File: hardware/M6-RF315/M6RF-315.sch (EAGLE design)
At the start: 38 parts, among them J1 CON-71439-2164, M1 MOUNT-HOLE3.3, M2 MOUNT-HOLE3.3, M3 MOUNT-HOLE3.3, M4 MOUNT-HOLE3.3, M5 FIDUCIAL1X2, M6 FIDUCIAL1X2, M7 FIDUCIAL1X2, M8 FIDUCIAL1X2, U1 CC1101RTKR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

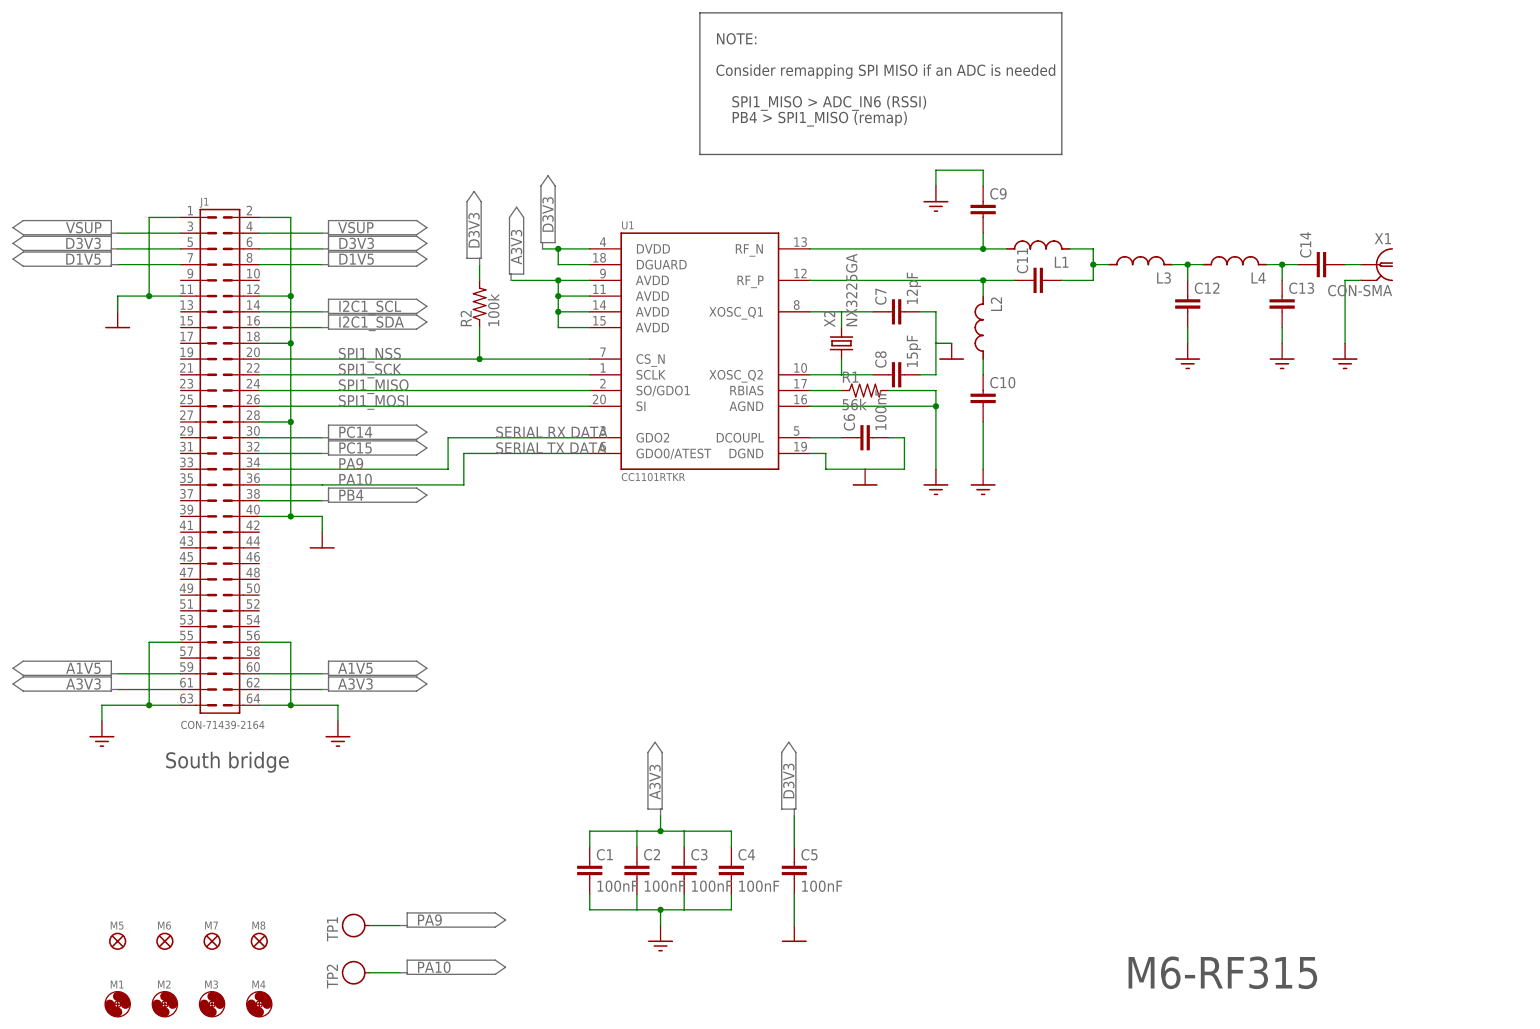
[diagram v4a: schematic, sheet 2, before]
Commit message: Modified GPIO-serial data connection, added LEDs, updated and cleaned up the library, defined antenna circuit component values and added datasheet..
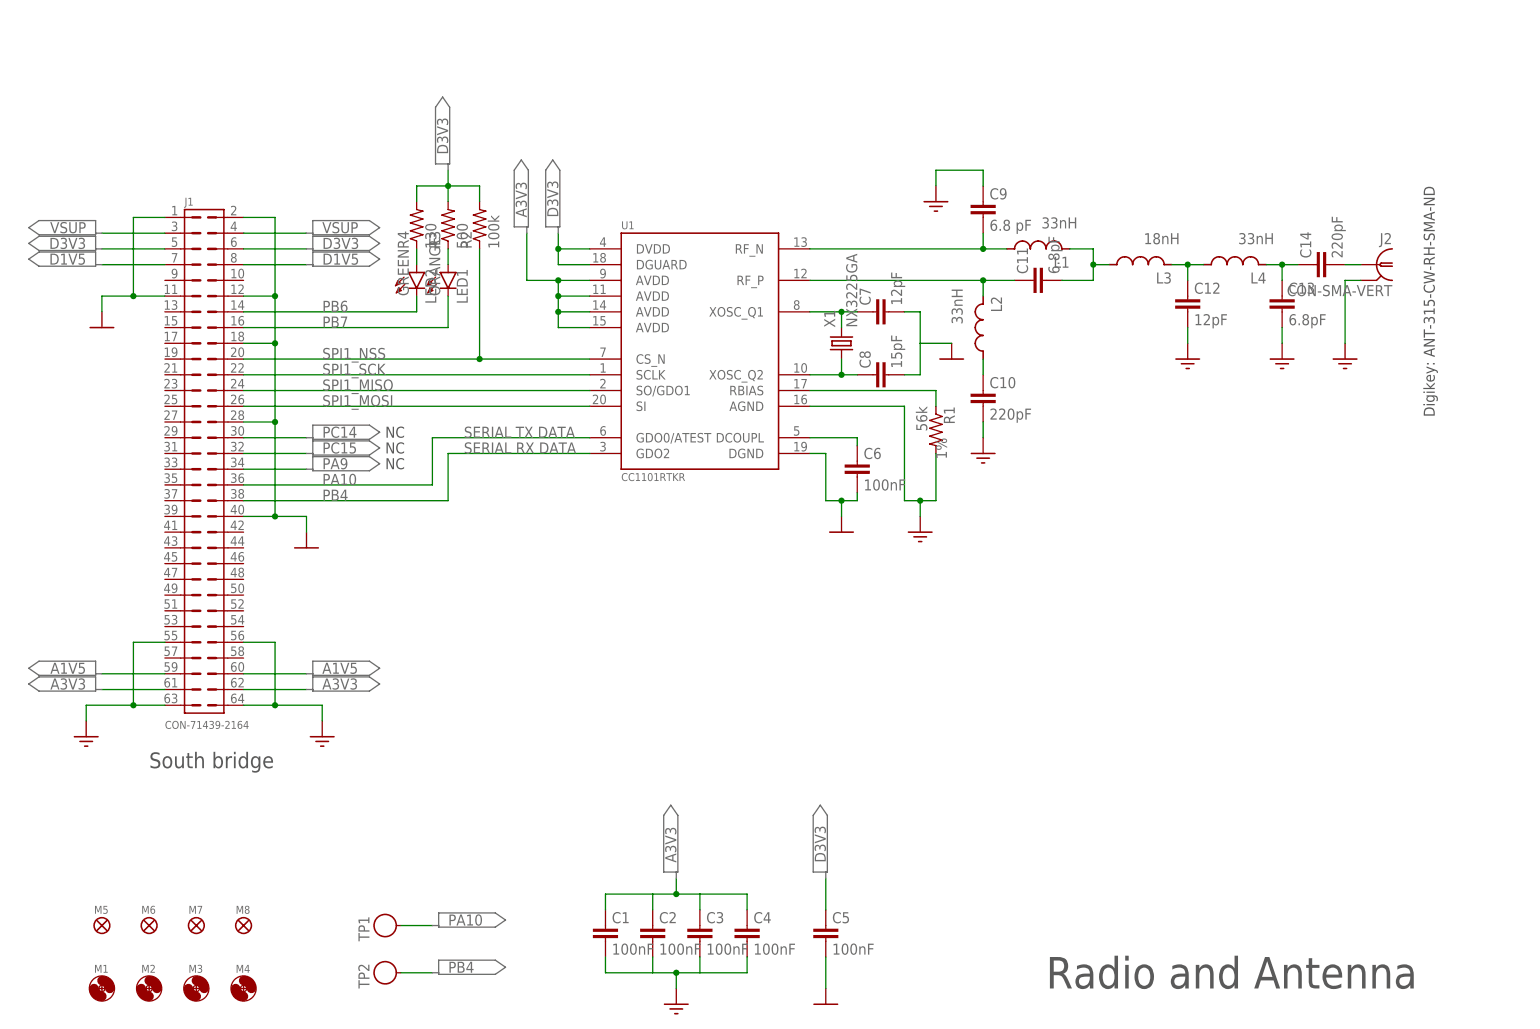
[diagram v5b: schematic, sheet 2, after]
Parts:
- removed X2: NX3225GA, M6-RF315:NX3225GA
- added J2: CON-SMA-VERT, M6-RF315:CON-SMA-VERT
- added LED1, LED2: (no value), M6-RF315:LED0603
- added R3: 500, M6-RF315:R0603
- added R4: 130, M6-RF315:R0603
- C10: value (none) -> 220pF; FUNCTION (none) -> RF balun DC blocking capacitor
- C11: value (none) -> 6.8pF; FUNCTION (none) -> RF balun/matching capacitors
- C12: value (none) -> 12pF; FUNCTION (none) -> RF LC filter/matching filter capacitor
- C13: value (none) -> 6.8pF; FUNCTION (none) -> RF LC filter/matching capacitor
- C14: value (none) -> 220pF; FUNCTION (none) -> RF LC filter DC blocking capacitor
- C9: value (none) -> 6.8 pF; FUNCTION (none) -> RF balun/matching capacitor
- L1, L2: value (none) -> 33nH; FUNCTION (none) -> RF balun/matching inductor
- L3: value (none) -> 18nH; FUNCTION (none) -> RF LC filter/matching filter inductor
- L4: value (none) -> 33nH; FUNCTION (none) -> RF LC filter/matching filter inductor
- R1: TOLERANCE (none) -> 1%
- X1: value CON-SMA -> NX3225GA; device M6-RF315:CON-SMA -> M6-RF315:NX3225GA
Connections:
- removed net I2C1_SCL: J1.14
- removed net I2C1_SDA: J1.16
- removed net N$5: C6.2
- new net N$19: LED2.A, R4.1
- new net PB6: J1.14, LED2.C
- new net PB7: J1.16, LED1.C
- net AGND: now also J2G$1.GND; no longer X1G$1.GND
- net D3V3: now also R3.2, R4.2
- net DGND: now also C6.2
- net N$1: now also LED1.A, R3.1; no longer J1.34, U1.GDO2
- net N$12: now also J2G$1.1; no longer X1G$1.1
- net N$6: now also X1.1; no longer X2.1
- net N$7: now also X1.2; no longer X2.2
- net PA10: now also TP1.1, U1.GDO0/ATEST; no longer TP2.1
- net PA9: now also J1.34; no longer TP1.1, U1.GDO0/ATEST
- net PB4: now also TP2.1, U1.GDO2
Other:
- note added: "- Check BOM against CC1101 reference BOM for 315 MHz"
- note added: "- Create BOM file"
- note added: "- Route PCB design"
- note added: "NC"
- note removed: "- Antenna matching circuit values"
- note removed: "- CC1101 PCB layout recommendations (footprint)"
- note removed: "- GND planes"
- note removed: "- Rbias value"
- note removed: "- TX/RX LEDs on I2C/PB4 (optional)"
- note removed: "Consider remapping SPI MISO if an ADC is needed"
- note removed: "NOTE:"
- note removed: "PB4 > SPI1_MISO (remap)"
- note removed: "SPI1_MISO > ADC_IN6 (RSSI)"
- moved on the sheet: C1, C2, C3, C4, C5, C6, C7, C8, J1, M1, M2, M3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

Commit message: M6-RF315 board 80% routed (9 airwires remaining).
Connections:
- net N$3 renamed RBIAS
- net AGND: now also J2G.GND@1, J2G.GND@2, J2G.GND@3
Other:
- moved on the sheet: C12, C13
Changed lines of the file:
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@@
 <attribute name="FUNCTION" x="175.26" y="134.62" size="1.778" layer="96" rot="R90" display="off"/>
 </instance>
-<instance part="C12" gate="G$1" x="200.66" y="132.08">
-<attribute name="FUNCTION" x="200.66" y="132.08" size="1.778" layer="96" display="off"/>
-</instance>
-<instance part="C13" gate="G$1" x="215.9" y="132.08">
-<attribute name="FUNCTION" x="215.9" y="132.08" size="1.778" layer="96" display="off"/>
+<instance part="C12" gate="G$1" x="200.66" y="130.81">
+<attribute name="FUNCTION" x="200.66" y="130.81" size="1.778" layer="96" display="off"/>
+</instance>
+<instance part="C13" gate="G$1" x="215.9" y="130.81">
+<attribute name="FUNCTION" x="215.9" y="130.81" size="1.778" layer="96" display="off"/>
 </instance>
 <instance part="C14" gate="G$1" x="220.98" y="137.16" rot="R90">
@@
 <attribute name="FUNCTION" x="208.28" y="137.16" size="1.778" layer="96" rot="R90" display="off"/>
 </instance>
-<instance part="U$9" gate="G$1" x="215.9" y="121.92"/>
+<instance part="U$9" gate="G$1" x="215.9" y="119.38"/>
 <instance part="U$12" gate="G$1" x="167.64" y="106.68"/>
-<instance part="U$13" gate="G$1" x="200.66" y="121.92"/>
-<instance part="U$14" gate="G$1" x="226.06" y="121.92"/>
+<instance part="U$13" gate="G$1" x="200.66" y="119.38"/>
+<instance part="U$14" gate="G$1" x="226.06" y="119.38"/>
 <instance part="X1" gate="G$1" x="144.78" y="127" rot="R90"/>
 <instance part="PORT10" gate="G$1" x="68.58" y="71.12"/>
@@
 <instance part="PORT2" gate="G$1" x="88.9" y="30.48"/>
 <instance part="PORT7" gate="G$1" x="88.9" y="22.86"/>
+<instance part="J2" gate="G" x="233.68" y="124.46" rot="R180"/>
 </instances>
 <busses>
@@
 <pinref part="C13" gate="G$1" pin="2"/>
 <pinref part="U$9" gate="G$1" pin="AGND"/>
-<wire x1="215.9" y1="127" x2="215.9" y2="124.46" width="0.1524" layer="91"/>
+<wire x1="215.9" y1="125.73" x2="215.9" y2="121.92" width="0.1524" layer="91"/>
 </segment>
 <segment>
@@
 <segment>
 <pinref part="C12" gate="G$1" pin="2"/>
-<wire x1="200.66" y1="127" x2="200.66" y2="124.46" width="0.1524" layer="91"/>
+<wire x1="200.66" y1="125.73" x2="200.66" y2="121.92" width="0.1524" layer="91"/>
 <pinref part="U$13" gate="G$1" pin="AGND"/>
 </segment>
@@
 <pinref part="J2" gate="G$1" pin="GND"/>
 <wire x1="228.6" y1="134.62" x2="226.06" y2="134.62" width="0.1524" layer="91"/>
-<wire x1="226.06" y1="124.46" x2="226.06" y2="134.62" width="0.1524" layer="91"/>
+<wire x1="226.06" y1="121.92" x2="226.06" y2="124.46" width="0.1524" layer="91"/>
 <pinref part="U$14" gate="G$1" pin="AGND"/>
+<pinref part="J2" gate="G" pin="GND@3"/>
+<wire x1="226.06" y1="124.46" x2="226.06" y2="127" width="0.1524" layer="91"/>
+<wire x1="226.06" y1="127" x2="226.06" y2="129.54" width="0.1524" layer="91"/>
+<wire x1="226.06" y1="129.54" x2="226.06" y2="134.62" width="0.1524" layer="91"/>
+<wire x1="231.14" y1="129.54" x2="226.06" y2="129.54" width="0.1524" layer="91"/>
+<pinref part="J2" gate="G" pin="GND@2"/>
+<wire x1="231.14" y1="127" x2="226.06" y2="127" width="0.1524" layer="91"/>
+<pinref part="J2" gate="G" pin="GND@1"/>
+<wire x1="231.14" y1="124.46" x2="226.06" y2="124.46" width="0.1524" layer="91"/>
+<junction x="226.06" y="124.46"/>
+<junction x="226.06" y="127"/>
+<junction x="226.06" y="129.54"/>
 </segment>
 <segment>
@@
 </segment>
 </net>
-<net name="N$3" class="0">
+<net name="RBIAS" class="0">
 <segment>
 <pinref part="U1" gate="G$1" pin="RBIAS"/>
@@
 <pinref part="C12" gate="G$1" pin="1"/>
 <pinref part="L3" gate="G$1" pin="2"/>
-<wire x1="200.66" y1="134.62" x2="200.66" y2="137.16" width="0.1524" layer="91"/>
+<wire x1="200.66" y1="133.35" x2="200.66" y2="137.16" width="0.1524" layer="91"/>
 <wire x1="200.66" y1="137.16" x2="198.12" y2="137.16" width="0.1524" layer="91"/>
 <pinref part="L4" gate="G$1" pin="1"/>
@@
 <pinref part="C13" gate="G$1" pin="1"/>
 <wire x1="215.9" y1="137.16" x2="218.44" y2="137.16" width="0.1524" layer="91"/>
-<wire x1="215.9" y1="134.62" x2="215.9" y2="137.16" width="0.1524" layer="91"/>
+<wire x1="215.9" y1="133.35" x2="215.9" y2="137.16" width="0.1524" layer="91"/>
 <junction x="215.9" y="137.16"/>
 </segment>
